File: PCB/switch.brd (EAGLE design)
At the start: 33 x 55.1 mm, 2 parts

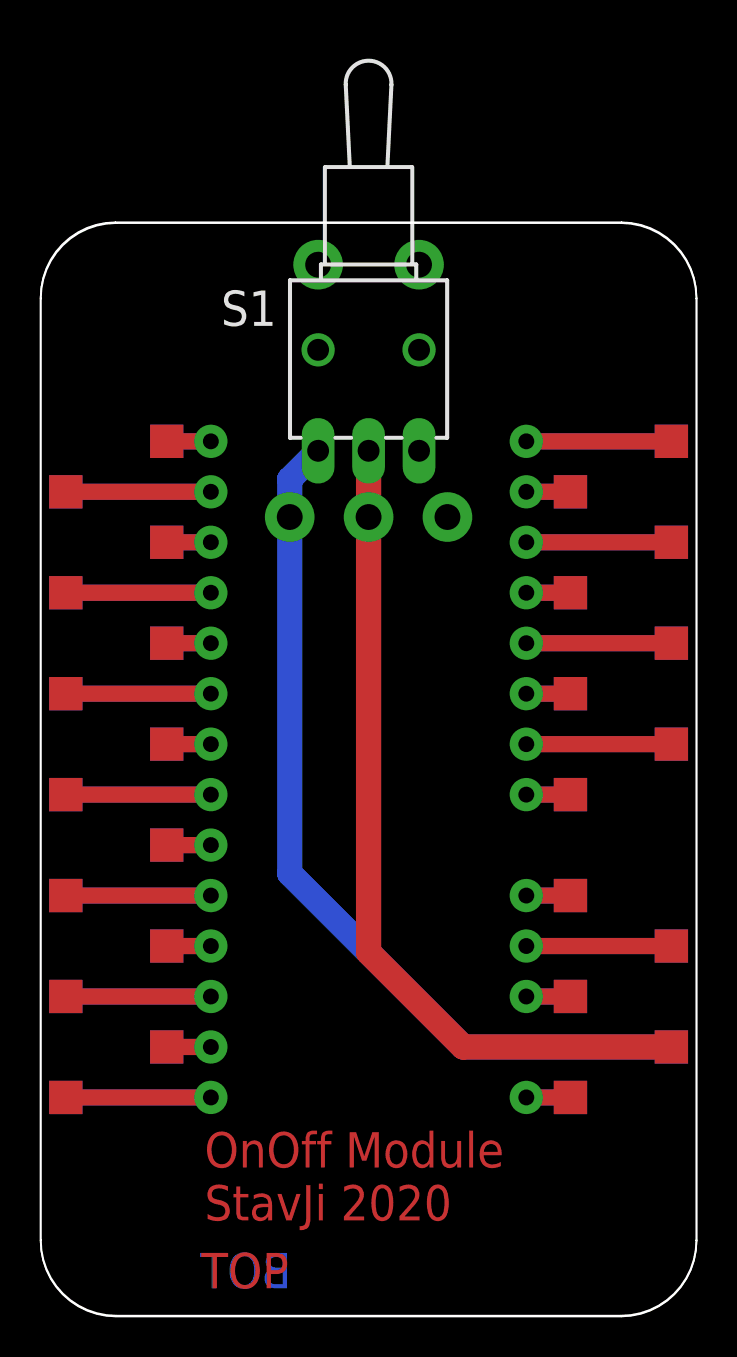
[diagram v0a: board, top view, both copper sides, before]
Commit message: feat: add header package ontline
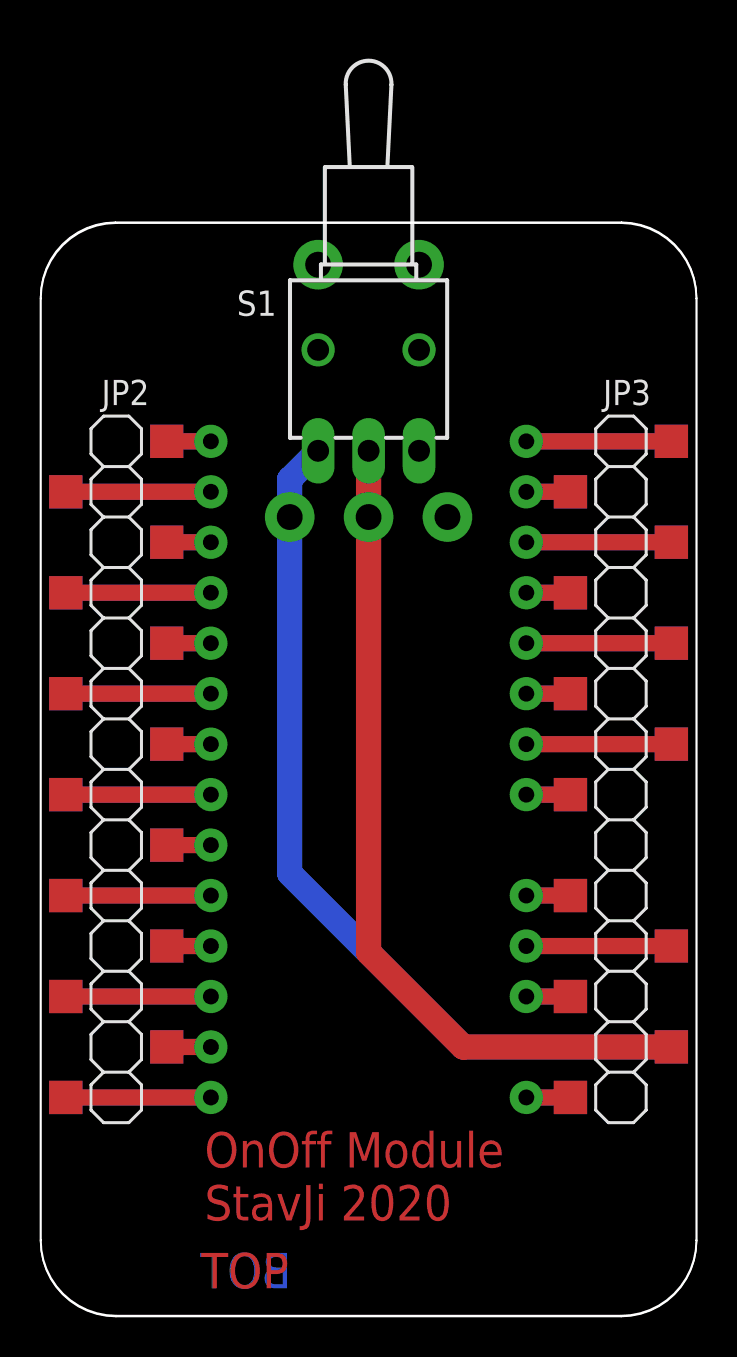
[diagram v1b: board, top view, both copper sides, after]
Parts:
- added JP2, JP4: 1-215297-4, pinhead:1X14_WITHOUT_PAD
- added JP3, JP5: 2211SM-14G-B1-TB, pinhead:1X14_WITHOUT_PAD
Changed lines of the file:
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@@
 <setting verticaltext="up"/>
 </settings>
-<grid distance="12.5" unitdist="mil" unit="mm" style="lines" multiple="1" display="yes" altdistance="0.025" altunitdist="inch" altunit="inch"/>
+<grid distance="6.25" unitdist="mil" unit="mil" style="lines" multiple="1" display="yes" altdistance="0.025" altunitdist="inch" altunit="inch"/>
 <layers>
 <layer number="1" name="Top" color="4" fill="1" visible="yes" active="yes"/>
@@
 <text x="12.620625" y="1.349375" size="1.778" layer="16" font="vector" ratio="12" rot="MR0">BOT</text>
 <text x="8.09625" y="1.349375" size="1.778" layer="1" font="vector" ratio="12">TOP</text>
-<text x="8.255" y="4.7625" size="1.778" layer="1">OnOff Module
+<text x="8.255" y="4.7625" size="1.778" layer="1" font="vector">OnOff Module
 StavJi 2020</text>
 </plain>
@@
 </element>
 <element name="S1" library="switch" package="TL3XWO" value="7101MD9AQE" x="16.51" y="48.5775" smashed="yes">
-<attribute name="NAME" x="11.8745" y="51.562" size="1.778" layer="25" rot="R180"/>
+<attribute name="NAME" x="11.8745" y="51.562" size="1.27" layer="25" font="vector" ratio="10" rot="R180"/>
 <attribute name="VALUE" x="22.86" y="44.0055" size="1.778" layer="27" rot="R90"/>
 </element>
+<element name="JP2" library="pinhead" package="1X14_WITHOUT_PAD" value="1-215297-4" x="3.81" y="27.46375" smashed="yes" rot="R90">
+<attribute name="NAME" x="5.4737" y="47.0662" size="1.27" layer="25" font="vector" ratio="10" rot="R180"/>
+<attribute name="VALUE" x="6.985" y="9.68375" size="1.27" layer="27" rot="R90"/>
+</element>
+<element name="JP3" library="pinhead" package="1X14_WITHOUT_PAD" value="2211SM-14G-B1-TB" x="29.21" y="27.46375" smashed="yes" rot="R90">
+<attribute name="NAME" x="30.71495" y="47.0662" size="1.27" layer="25" font="vector" ratio="10" rot="R180"/>
+<attribute name="VALUE" x="32.385" y="9.68375" size="1.27" layer="27" rot="R90"/>
+</element>
+<element name="JP4" library="pinhead" package="1X14_WITHOUT_PAD" value="1-215297-4" x="3.81" y="27.46375" smashed="yes" rot="MR90">
+<attribute name="NAME" x="5.4737" y="7.70255" size="1.27" layer="26" font="vector" ratio="10" rot="MR0"/>
+<attribute name="VALUE" x="0.635" y="9.68375" size="1.27" layer="28" rot="MR90"/>
+</element>
+<element name="JP5" library="pinhead" package="1X14_WITHOUT_PAD" value="2211SM-14G-B1-TB" x="29.21" y="27.46375" smashed="yes" rot="MR90">
+<attribute name="NAME" x="31.03245" y="7.8613" size="1.27" layer="26" font="vector" ratio="10" rot="MR0"/>
+<attribute name="VALUE" x="26.035" y="9.68375" size="1.27" layer="28" rot="MR90"/>
+</element>
 </elements>

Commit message: fix: switch package ontline
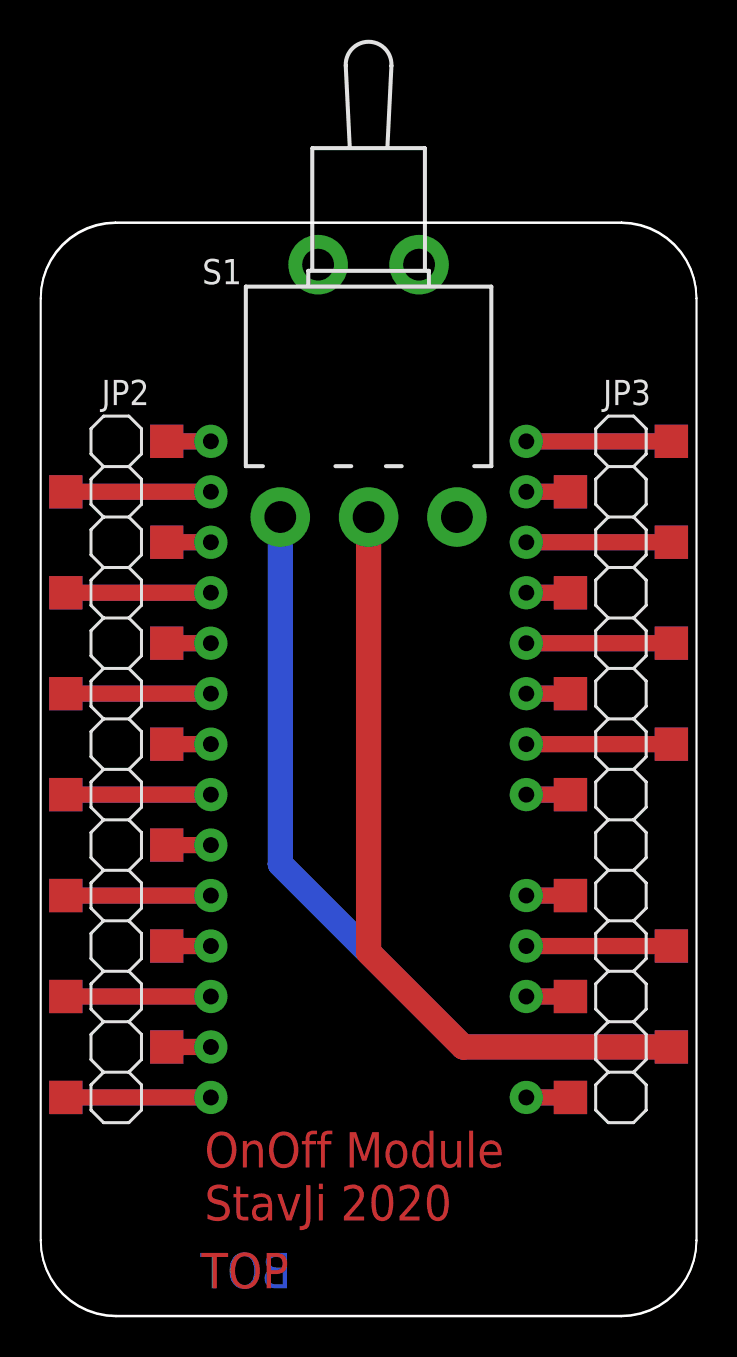
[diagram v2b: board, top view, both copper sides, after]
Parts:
- S1: value 7101MD9AQE -> TL32WOSWITCH; device switch:TL3XWO -> switch:SWITCH
- moved S1 0.79 mm to (16.5, 47.8)
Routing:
- net N$32: track 44.7 -> 41.0 mm, vias 1 -> 0
- net N$33: track 42.5 -> 39.1 mm, vias 1 -> 0
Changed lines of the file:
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@@
 <setting verticaltext="up"/>
 </settings>
-<grid distance="6.25" unitdist="mil" unit="mil" style="lines" multiple="1" display="yes" altdistance="0.025" altunitdist="inch" altunit="inch"/>
+<grid distance="6.25" unitdist="mil" unit="mm" style="lines" multiple="1" display="yes" altdistance="0.025" altunitdist="inch" altunit="inch"/>
 <layers>
 <layer number="1" name="Top" color="4" fill="1" visible="yes" active="yes"/>
@@
 <attribute name="VALUE" x="16.51" y="26.46375" size="1.5" layer="27" align="center"/>
 </element>
-<element name="S1" library="switch" package="TL3XWO" value="7101MD9AQE" x="16.51" y="48.5775" smashed="yes">
-<attribute name="NAME" x="11.8745" y="51.562" size="1.27" layer="25" font="vector" ratio="10" rot="R180"/>
-<attribute name="VALUE" x="22.86" y="44.0055" size="1.778" layer="27" rot="R90"/>
-</element>
 <element name="JP2" library="pinhead" package="1X14_WITHOUT_PAD" value="1-215297-4" x="3.81" y="27.46375" smashed="yes" rot="R90">
 <attribute name="NAME" x="5.4737" y="47.0662" size="1.27" layer="25" font="vector" ratio="10" rot="R180"/>
@@
 <attribute name="VALUE" x="26.035" y="9.68375" size="1.27" layer="28" rot="MR90"/>
 </element>
+<element name="S1" library="switch" package="SWITCH" value="TL32WOSWITCH" x="16.51" y="47.78375" smashed="yes">
+<attribute name="NAME" x="10.12825" y="53.1495" size="1.27" layer="25" font="vector" ratio="10" rot="R180"/>
+<attribute name="VALUE" x="24.92375" y="43.21175" size="1.778" layer="27" rot="R90"/>
+</element>
 </elements>
 <signals>
@@
 </signal>
 <signal name="N$32">
-<via x="12.54125" y="40.16375" extent="1-16" drill="1.3" diameter="2.5"/>
 <contactref element="JP1" pad="16B"/>
 <wire x1="31.75" y1="13.49375" x2="21.2725" y2="13.49375" width="1.27" layer="16"/>
-<wire x1="21.2725" y1="13.49375" x2="12.54125" y2="22.225" width="1.27" layer="16"/>
-<wire x1="12.54125" y1="40.16375" x2="12.54125" y2="22.225" width="1.27" layer="16"/>
+<wire x1="21.2725" y1="13.49375" x2="12.065" y2="22.70125" width="1.27" layer="16"/>
+<wire x1="12.065" y1="40.16375" x2="12.065" y2="22.70125" width="1.27" layer="16"/>
 <contactref element="S1" pad="1"/>
-<wire x1="12.54125" y1="40.16375" x2="12.54125" y2="42.06875" width="1.27" layer="16"/>
-<wire x1="12.54125" y1="42.06875" x2="13.97" y2="43.4975" width="1.27" layer="16"/>
 </signal>
 <signal name="N$33">
-<via x="16.51" y="40.16375" extent="1-16" drill="1.3" diameter="2.5"/>
 <contactref element="JP1" pad="16"/>
 <wire x1="31.75" y1="13.49375" x2="21.2725" y2="13.49375" width="1.27" layer="1"/>
@@
 <wire x1="16.51" y1="40.16375" x2="16.51" y2="18.25625" width="1.27" layer="1"/>
 <contactref element="S1" pad="2"/>
-<wire x1="16.51" y1="40.16375" x2="16.51" y2="43.4975" width="1.27" layer="1"/>
-</signal>
-<signal name="N$34">
-<via x="20.47875" y="40.16375" extent="1-16" drill="1.3" diameter="2.5"/>
-</signal>
-<signal name="N$29">
-<via x="13.97" y="52.86375" extent="1-16" drill="1.3" diameter="2.5"/>
-</signal>
-<signal name="N$30">
-<via x="19.05" y="52.86375" extent="1-16" drill="1.3" diameter="2.5"/>
 </signal>
 </signals>
